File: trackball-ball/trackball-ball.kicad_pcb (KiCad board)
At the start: 4 copper layers, 27.5 x 27.5 mm, 92 parts, among them J1 FH28D-28S, J2 JST-PH-3, J3 JST-PH-2, Q1 DMG6968U, U1 NRF52810-QCAA, U2 CY8CMBR3116-0x37, U3 CY8CMBR3116-0x38, U4 LTC4120-4.2, U5 BQ29700, U6 XC6206P302, Y1 32MHz-CL9pF

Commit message: ball: driver-preserved WIP — 21g (s)-via-form cleared (1 op ...500 97.7->96.45), QUESTIONS 21g + PROGRESS (WIP, NOT clean)
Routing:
- net I2C_SDA: track 57.3 -> 56.0 mm
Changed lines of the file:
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@@
   (segment (start 104.25 97.15) (end 104.25 97.6) (width 0.25) (layer "F.Cu") (net 3))
   (segment (start 104.25 97.15) (end 105.9 97.15) (width 0.25) (layer "F.Cu") (net 3))
-  (segment (start 97.7 97.75) (end 96.3 97.75) (width 0.25) (layer "F.Cu") (net 32))
+  (segment (start 96.45 97.75) (end 96.3 97.75) (width 0.25) (layer "F.Cu") (net 32))
   (via (at 96.3 97.75) (size 0.6) (drill 0.3) (layers "F.Cu" "B.Cu") (net 32))
   (segment (start 96.3 97.75) (end 96.3 98) (width 0.25) (layer "B.Cu") (net 32))

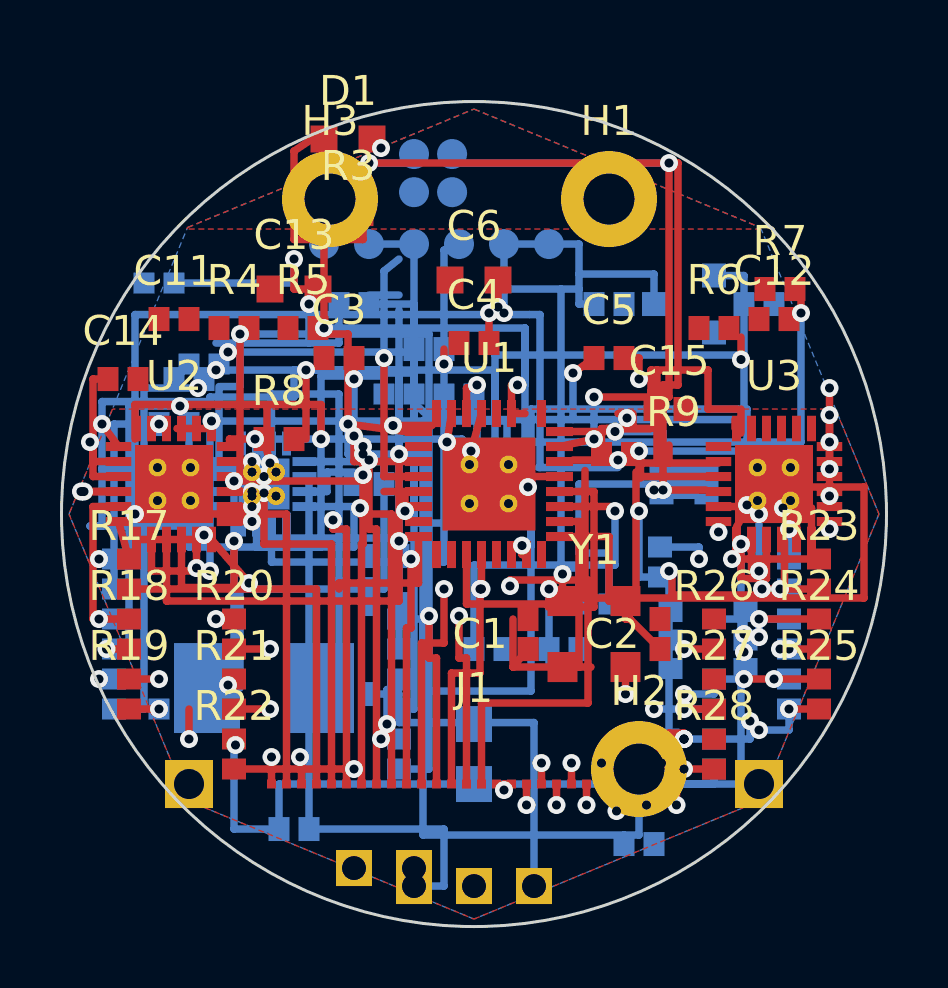
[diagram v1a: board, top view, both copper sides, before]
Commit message: ball: driver gate-9 DRC/ERC recount 2026-10-14 (knot WIP preserved, NOT clean)
Knot 13-op fix + Q-H/(n) filings committed as driver-preserved WIP per
delegate request (commit TOOL-RUN-TBD, no shell on delegate side).

Fresh tool counts (kicad-cli 10.0.6, --refill-zones --schematic-parity):
  ERC: 510 violations (flat vs standing baseline)
  DRC: 1748 violations / 63 unconnected / 92 parity
  vs gate-7 baseline (2026-10-13 21:48): 1739 / 87 / 92
  Unconnected distinct-item set UNCHANGED (87->63 is entry-count only).

Q32 kill-pairs all ABSENT from fresh runs (deletions landed):
  ...284-vs-...718, ...284-vs-J1.26, ...285/286/287-vs-H2, ...283-vs-...718.

NEW file-proven defects from knot copper (both fresh runs + geometry):
  1. ...903<->...712 shorting: T21(net29) B.Cu (105.5,102.1)->(108.5,102.1)
     vs SDA(net32) via (106.5,101.9) r0.3: 0.2 c-c < 0.425 -> 0.225 overlap.
  2. ...907<->...718 crossing: T23(net31) B.Cu (108,109)->(108,111)
     endpoint sits ON SCL(net33) (105.5,109)->(108.9,109): real contact.

Pair-level diff vs 2148 baseline NOT reliable: back-to-back DRC runs on
the identical file disagree on 45 pairs (clearance<->shorting<->hole
reclassification + re-pairing). (n) SDA<->SCL 1.0mm y109 collinear overlap
is file-real (delegate 2026-10-14 proof) but unflagged by fresh DRC runs.

Worker action: fix (1)+(2) under standing layout authority, file-verify,
then east-field In2 census one cluster/checkpoint. (WIP, NOT clean)
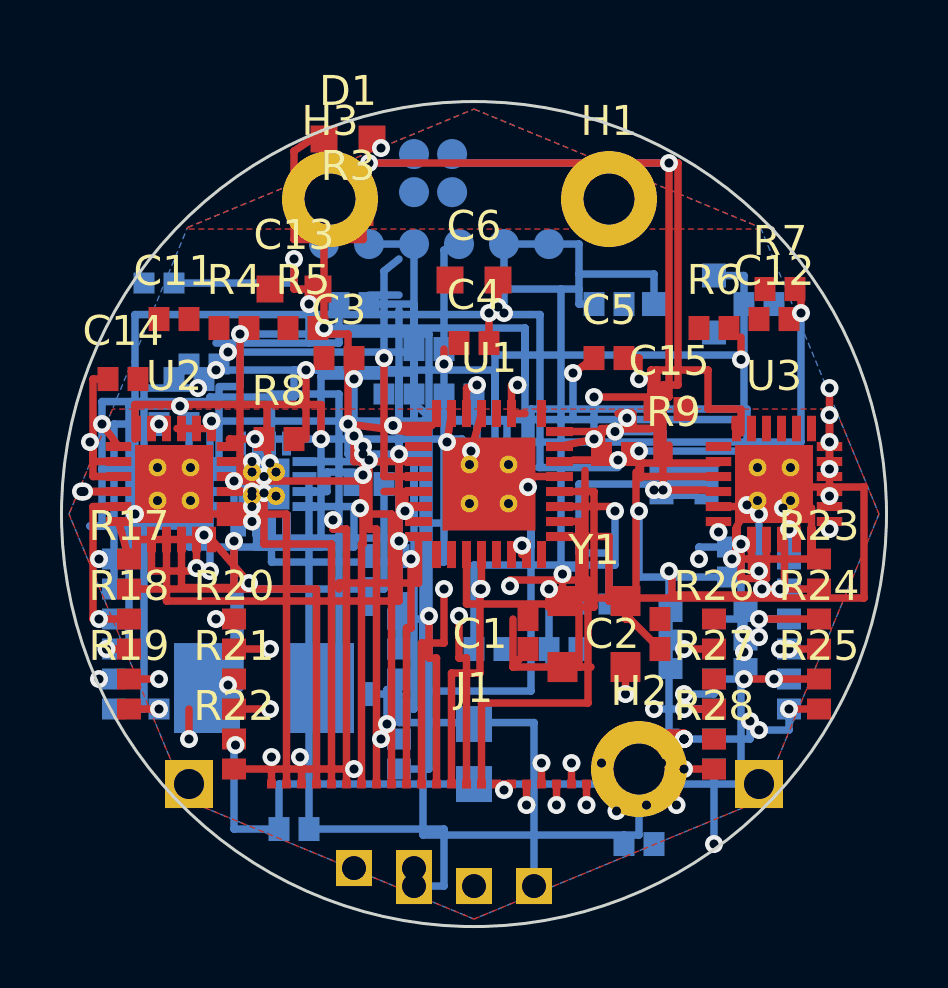
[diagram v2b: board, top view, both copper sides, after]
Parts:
- moved R38 2.30 mm to (108.5, 101.6)
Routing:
- net T21: track 14.5 -> 16.8 mm
- net T23: track 4.50 -> 5.15 mm
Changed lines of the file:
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@@
     (fp_rect (start -0.65 -1.05) (end 0.65 1.05) (stroke (width 0.05) (type solid)) (layer "B.CrtYd") (fill none))
   )
-  (footprint "Resistor_SMD:R_0402_1005Metric" (version 20250114) (generator "pcbnew") (generator_version "10.0") (layer "B.Cu") (at 106.2 101.6) (descr "R38 560R (moved 106.5,102->106.2,101.6: clears U3/Q1/C23 courtyards)") (tags "res")
+  (footprint "Resistor_SMD:R_0402_1005Metric" (version 20250114) (generator "pcbnew") (generator_version "10.0") (layer "B.Cu") (at 108.5 101.6) (descr "R38 560R (moved 106.5,102->106.2,101.6: clears U3/Q1/C23 courtyards; moved 106.2,101.6->108.5,101.6: I2C-knot (j) pads off SDA-711 corridor)") (tags "res")
     (property "Reference" "R38" (at 0 -1.6 0) (layer "B.SilkS") (effects (font (size 1 1) (thickness 0.15))))
     (property "Value" "560R-0402" (at 0 1.6 0) (layer "B.Fab") (effects (font (size 1 1) (thickness 0.15))))
@@
   (via (at 105.25 108.3) (size 0.6) (drill 0.3) (layers "F.Cu" "B.Cu") (net 28))
   (segment (start 105.25 108.3) (end 105.25 108.85) (width 0.25) (layer "F.Cu") (net 28))
-  (segment (start 106.2 102.1) (end 105.5 102.1) (width 0.25) (layer "B.Cu") (net 29))
+  (segment (start 105.5 102.1) (end 108.5 102.1) (width 0.25) (layer "B.Cu") (net 29))
   (segment (start 105.5 102.1) (end 105.5 99.9) (width 0.25) (layer "B.Cu") (net 29))
   (via (at 105.5 99.9) (size 0.6) (drill 0.3) (layers "F.Cu" "B.Cu") (net 29))
@@
   (segment (start 106.25 108.3) (end 106.25 108.85) (width 0.25) (layer "F.Cu") (net 30))
   (segment (start 108 108.5) (end 108 109) (width 0.25) (layer "B.Cu") (net 31))
-  (segment (start 108 109) (end 106 109) (width 0.25) (layer "B.Cu") (net 31))
-  (via (at 106 109) (size 0.6) (drill 0.3) (layers "F.Cu" "B.Cu") (net 31))
-  (segment (start 106 109) (end 106.5 109) (width 0.25) (layer "In2.Cu") (net 31))
-  (segment (start 106.5 109) (end 106.5 109.7) (width 0.25) (layer "In2.Cu") (net 31))
-  (segment (start 106.5 109.7) (end 106.75 109.7) (width 0.25) (layer "In2.Cu") (net 31))
+  (segment (start 108 109) (end 108 111) (width 0.25) (layer "B.Cu") (net 31))
+  (via (at 108 111) (size 0.6) (drill 0.3) (layers "F.Cu" "B.Cu") (net 31))
+  (segment (start 108 111) (end 106.9 111) (width 0.25) (layer "In2.Cu") (net 31))
+  (segment (start 106.9 111) (end 106.9 110) (width 0.25) (layer "In2.Cu") (net 31))
   (via (at 106.75 109.7) (size 0.6) (drill 0.3) (layers "F.Cu" "B.Cu") (net 31))
   (segment (start 106.75 109.7) (end 106.75 109.15) (width 0.25) (layer "F.Cu") (net 31))
@@
   (via (at 107.5 101.5) (size 0.6) (drill 0.3) (layers "F.Cu" "B.Cu") (net 75))
   (segment (start 107.5 101.5) (end 107.5 101.1) (width 0.25) (layer "B.Cu") (net 75))
-  (segment (start 107.5 101.1) (end 106.2 101.1) (width 0.25) (layer "B.Cu") (net 75))
+  (segment (start 107.5 101.1) (end 108.5 101.1) (width 0.25) (layer "B.Cu") (net 75))
   (segment (start 99.25 96.65) (end 99.1 97.6) (width 0.25) (layer "F.Cu") (net 34))
   (via (at 99.1 97.6) (size 0.6) (drill 0.3) (layers "F.Cu" "B.Cu") (net 34))
